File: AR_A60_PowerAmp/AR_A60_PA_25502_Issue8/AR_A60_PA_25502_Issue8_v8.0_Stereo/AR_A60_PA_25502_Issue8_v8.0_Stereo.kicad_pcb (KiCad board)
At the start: 2 copper layers, 180.3 x 128.3 mm, 157 parts, among them J1 Conn_01x04, J101 Conn_01x04, J2 J_HP_Left, J3 J_HP_Right, Q10 BC547, Q109 BC547, Q11 BC547, Q110 BC547, Q111 BC547, Q112 BC547, Q113 ZTX753, Q114 BC547, Q115 ZTX653, Q116 BC547, Q117 BC557, Q118 ZTX653, Q119 ZTX753, Q12 BC547, Q120 TIP3055, Q121 TIP3055, Q13 ZTX753, Q14 BC547, Q15 ZTX653, Q16 BC547, Q17 BC557, Q18 ZTX653, Q19 ZTX753, Q20 TIP3055, Q21 TIP3055, Q9 BC547, p1 Pad3_Hole1.5mm_Pad3.0mm_Pitch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, p101 Pad3_Hole1.5mm_Pad3.0mm_Pitch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

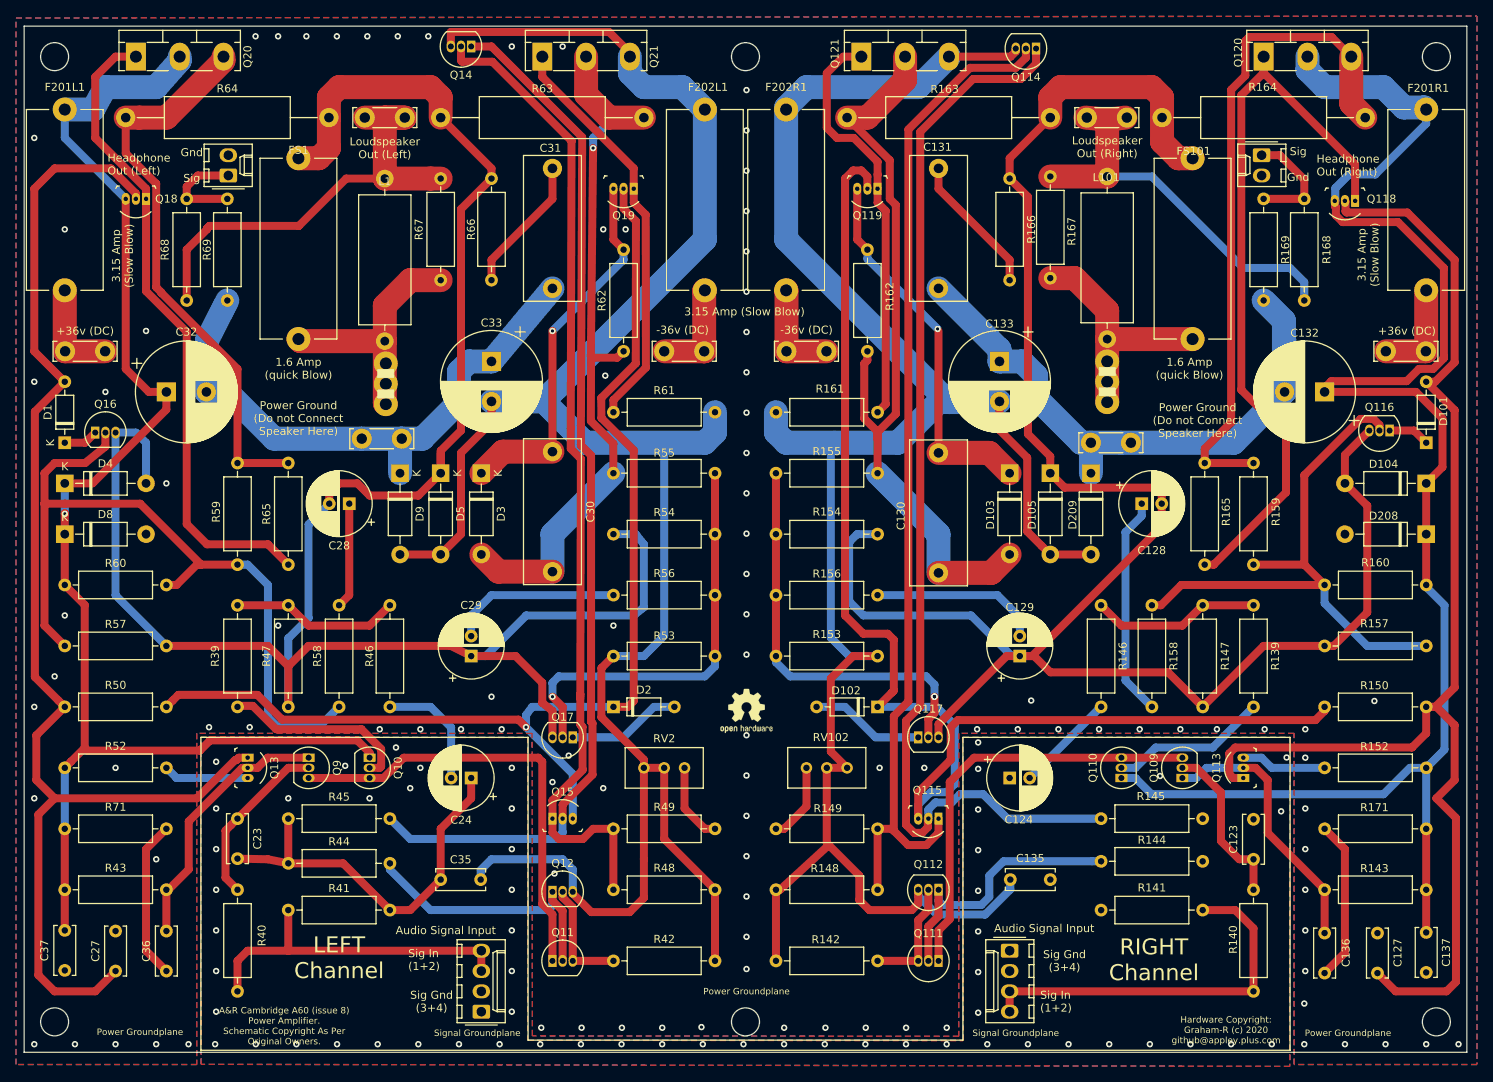
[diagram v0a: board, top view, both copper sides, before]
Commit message: Updated polycarb caps
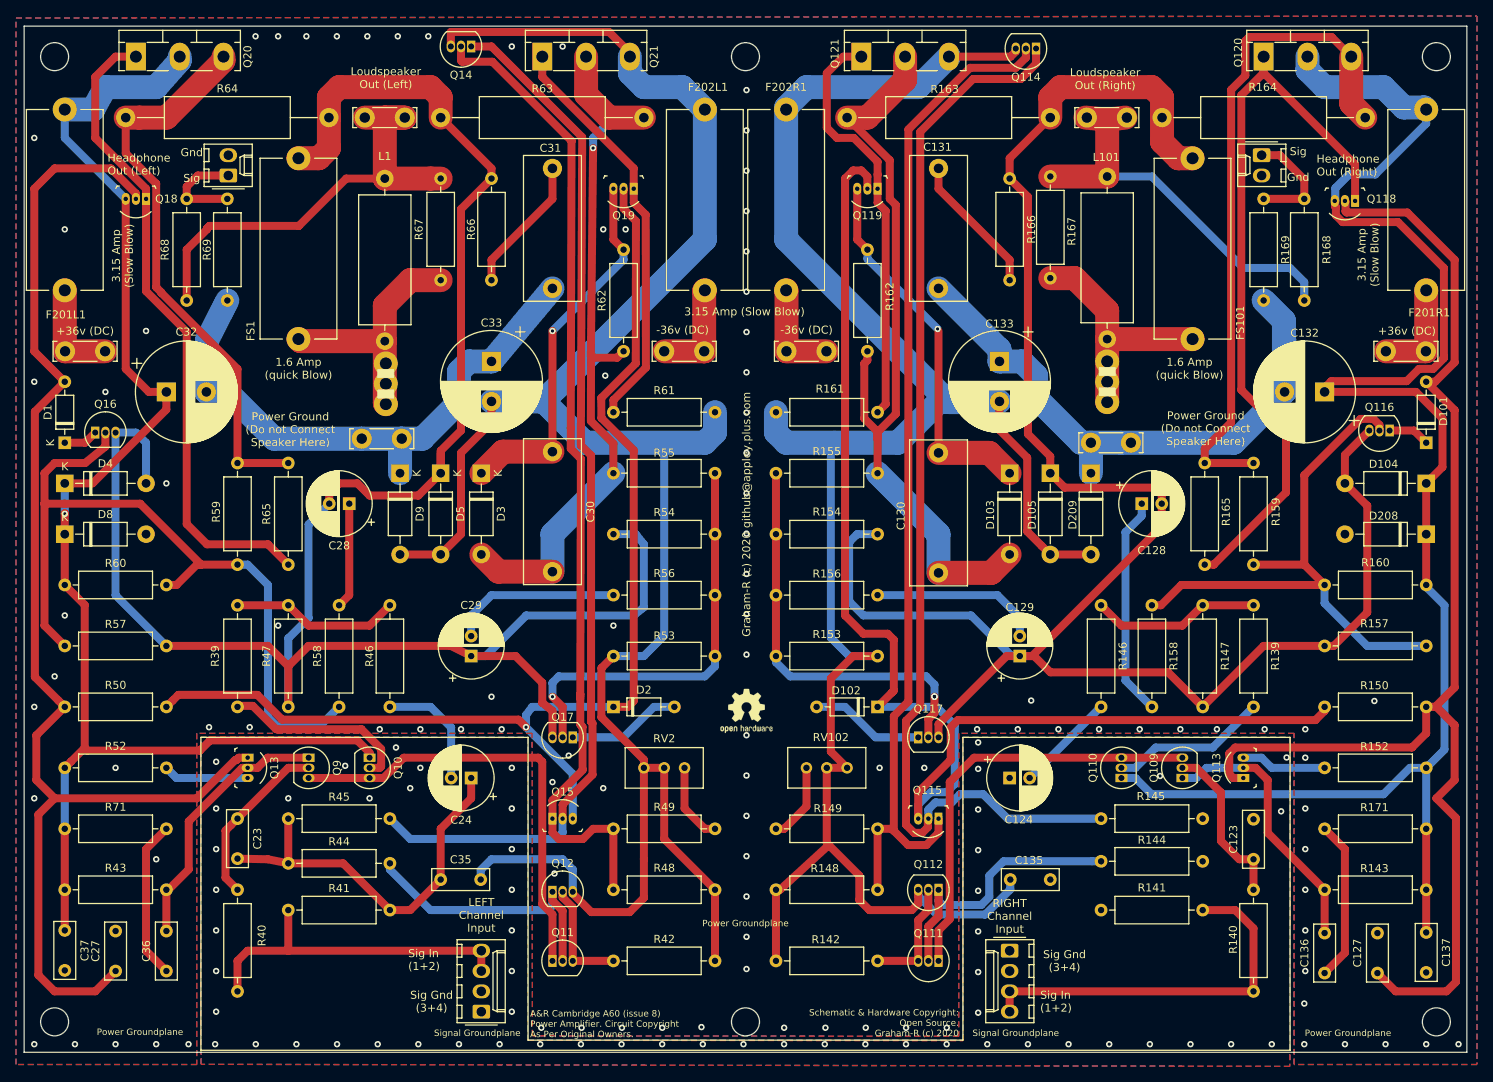
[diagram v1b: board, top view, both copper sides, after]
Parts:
- C123, C127, C135, C136, C137, C23, C27, C35, C36, C37: footprint Capacitor_THT:C_Disc_D6.0mm_W2.5mm_P5.00mm -> Capacitor_THT:C_Rect_L7.0mm_W2.5mm_P5.00mm
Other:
- board text added: "A&R Cambridge A60 (issue 8) Power Amplifier. Circuit Copyright As Per Original Owners."
- board text added: "Graham-R (c) 2020 github@appley.plus.com"
- board text added: "LEFT Channel Input"
- board text added: "RIGHT Channel Input"
- board text added: "Schematic & Hardware Copyright: Open Source. Graham-R (c) 2020"
- board text removed: "A&R Cambridge A60 (issue 8) Power Amplifier. Schematic Copyright As Per Original Owners."
- board text removed: "Audio Signal Input"
- board text removed: "Hardware Copyright: Graham-R (c) 2020 github@appley.plus.com"
- board text removed: "LEFT Channel"
- board text removed: "RIGHT Channel"
